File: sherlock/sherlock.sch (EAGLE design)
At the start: 24 parts, among them U3 XBEE-1B2, X1 2540-

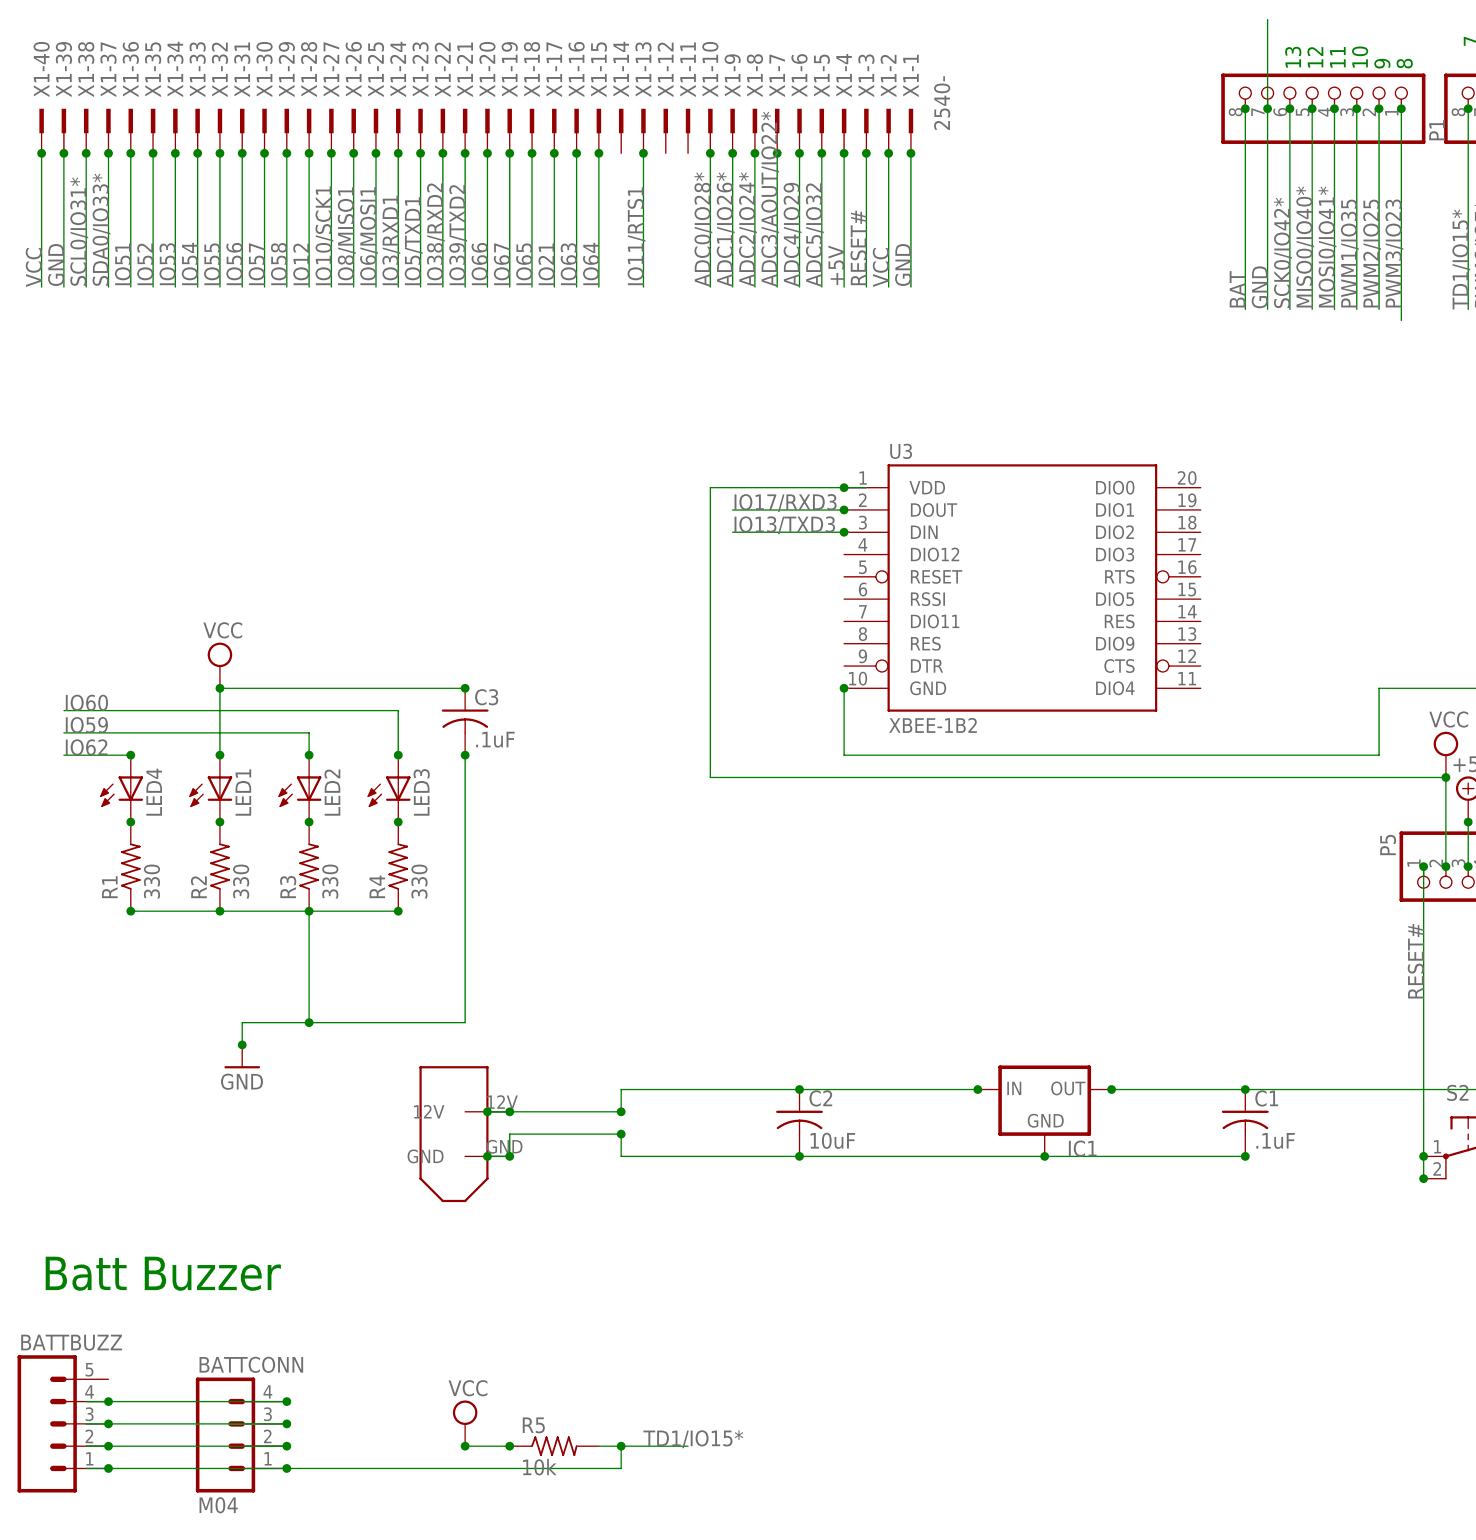
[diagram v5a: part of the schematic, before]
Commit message: Updated Sherlock, Watson & Solenoid Board to Rev D. Updated pie.lbr.
- Put SSOP16 footprint and symbol (from Sparkfun.lbr) in pie.lbr.
  Can be used as a template for any SSOP16 device.
- Created SSOP14 footprint and symbol in pie.lbr using SSOP16.
  Can be used as a template for any SSOP14 device.
- Added QUADNOR device to pie.lbr
- Added VCC and enable pin to solenoid connector on Watson
- Added enable pin for solenoid board on Sherlock
- Added quad-NOR gate onto Solenoid Board
- Added VCC and enable pin for quad-NOR gate on Solenoid Board
- Added 0.1uF capacitors between VCC&GND and 12V&GND for Solenoid Board
- Added mounting holes to Solenoid Board
- Added additional holes to Sherlock and Watson for the testing jig
- Replaced all holes with standoff part in pie.lbr
- Gave each hole a value, either "Mounting", "Test" or "Mounting + Test"
  to state their purpose.
- Added/copied devices on boards that were NOT in pie.lbr TO pie.lbr
- Removed unnecessary packages from copied devices
- Manually set pad diameters for through-hole packages that were
  added/created/already there for these three boards
- Added PARTNUMBER attribute to the library parts added/copied/
  created/already there for these three boards
- Moved all Sherlock passives to the top

RYAN: I fixed what you asked for this revision. If this goes
through, I will then work on fixing everything else you told me to.

Sherlock DFM: https://www.freedfm.com/freedfm/0019486703414971/results/summary2.htm
Watson DFM: https://www.freedfm.com/freedfm/0019486703414975/results/summary2.htm
Solenoid Board DFM: https://www.freedfm.com/freedfm/0019486703414973/results/summary2.htm

Change-Id: Ie6b1bdecadde8b7bc780ad23041f2e110bf24a4c
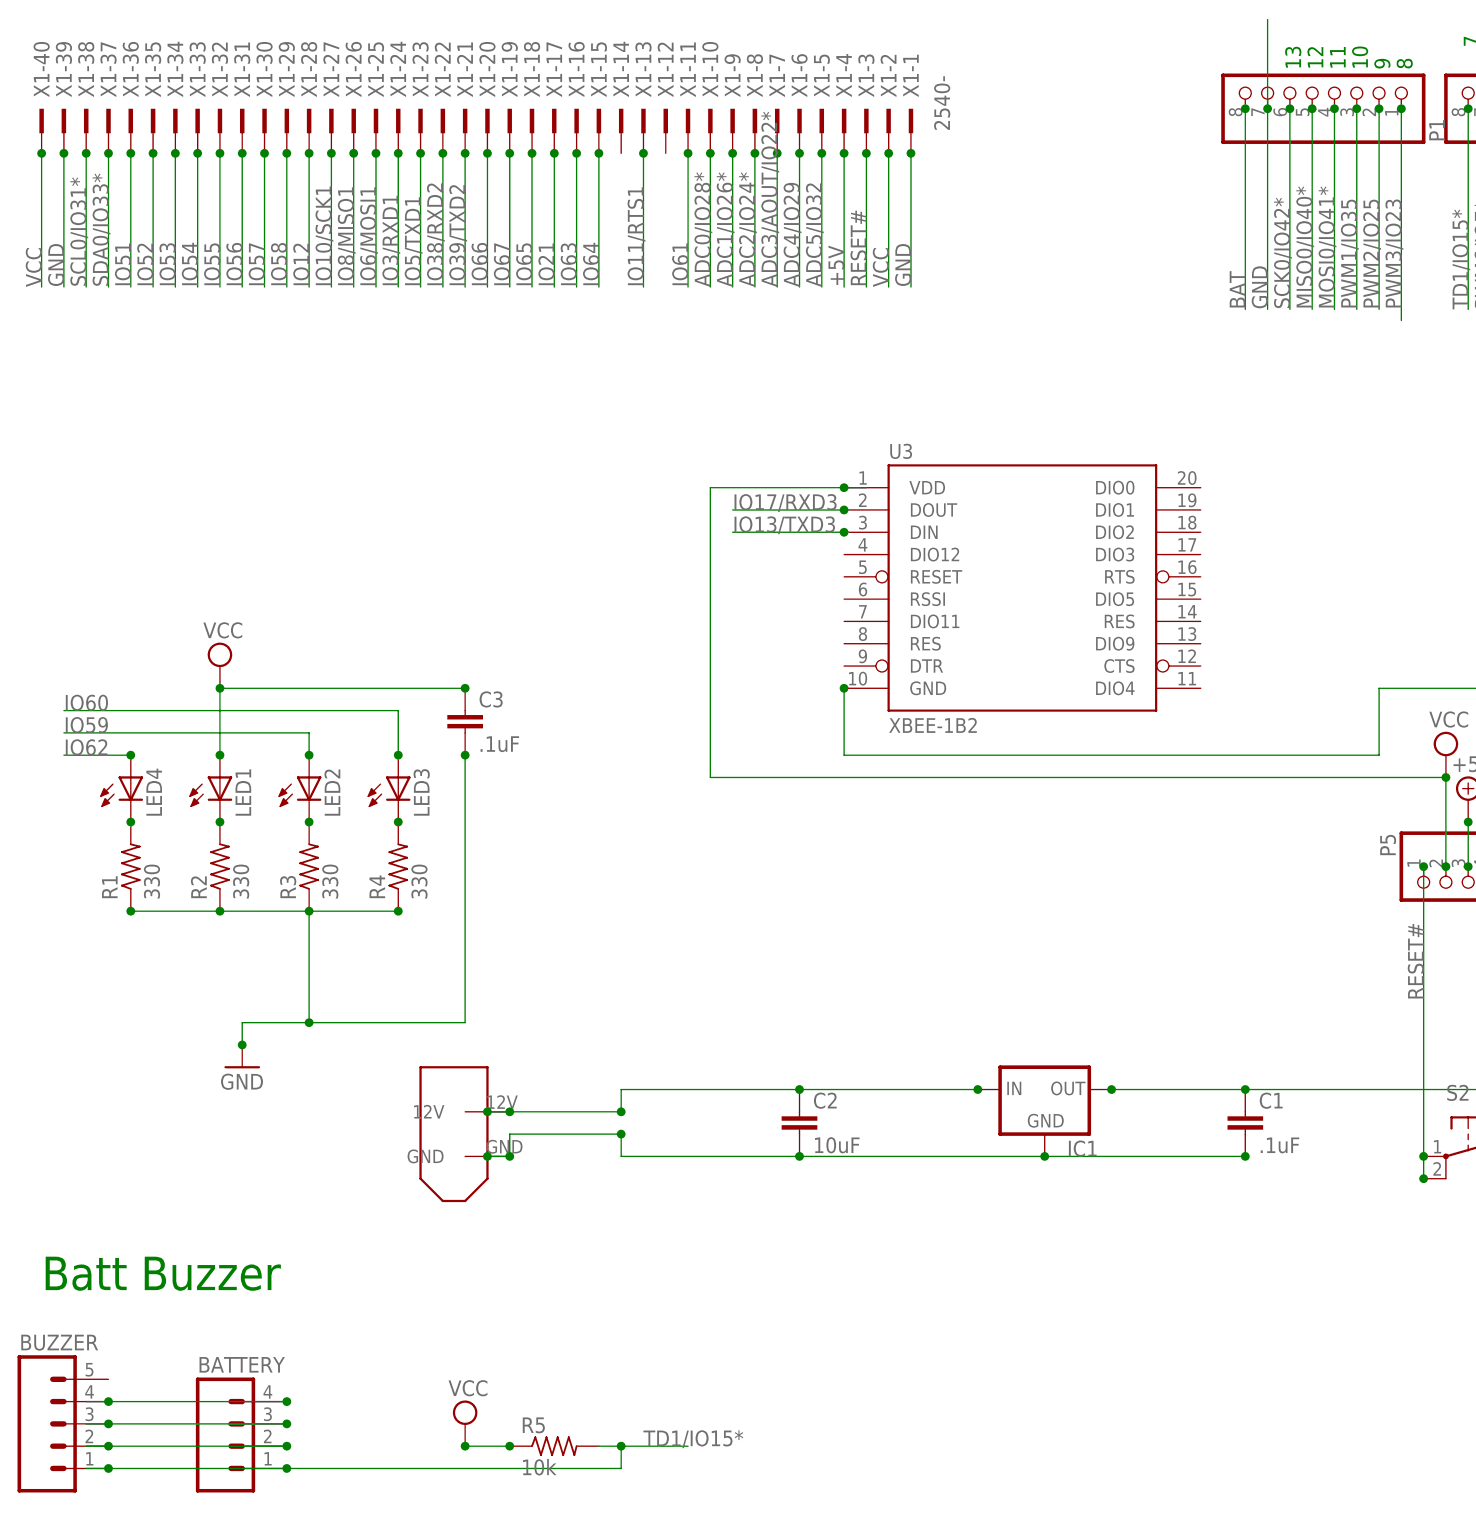
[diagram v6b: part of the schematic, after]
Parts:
- removed BATTBUZZ: (no value), SparkFun:M05PTH
- removed BATTCONN: M04, pie:M04
- added BATTERY: (no value), pie:M041X04-MTA
- added BUZZER: (no value), pie:M05PTH
- C1, C2: device rcl:C-USC0603 -> pie:CAP0603-CAP
- C3: device rcl:C-USC0603K -> pie:CAP0603-CAP
- IC1: device pie:78XXL -> pie:V_REG_78XXSIDE
- P1, P2: device pinhead-2:PINHD-1X08_2.54-S -> pie:PINHD-1X8
- P3: device pinhead:PINHD-2X20 -> pie:PINHD-2X20
- P4, P5: device pinhead-2:PINHD-1X06_2.54-S -> pie:PINHD-1X6
- R1, R2, R3, R4: device rcl:R-US_R0603 -> pie:R-US_R0603
- R5: device resistor:R-US_R0603 -> pie:R-US_R0603
- S2: device SparkFun:TAC_SWITCHPTH -> pie:TAC_SWITCHPTH
- U3: device SparkFun:XBEE-1B2 -> pie:XBEE-1B2
- X1: device con-3m:2540- -> pie:2540-
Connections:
- net IO61: now also X1-11.KL
- net N$5: now also BATTERY.4, BUZZER.4; no longer BATTBUZZ.4, BATTCONN.4
- net N$6: now also BATTERY.3, BUZZER.3; no longer BATTBUZZ.3, BATTCONN.3
- net N$7: now also BATTERY.2, BUZZER.2; no longer BATTBUZZ.2, BATTCONN.2
- net TD1/IO15*: now also BATTERY.1, BUZZER.1; no longer BATTBUZZ.1, BATTCONN.1
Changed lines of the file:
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@@
 </classes>
 <parts>
-<part name="P1" library="pinhead-2" deviceset="PINHD-1X08" device="_2.54-S"/>
-<part name="P2" library="pinhead-2" deviceset="PINHD-1X08" device="_2.54-S"/>
-<part name="P4" library="pinhead-2" deviceset="PINHD-1X06" device="_2.54-S"/>
-<part name="P5" library="pinhead-2" deviceset="PINHD-1X06" device="_2.54-S"/>
+<part name="P1" library="pie" deviceset="PINHD-1X8" device=""/>
+<part name="P2" library="pie" deviceset="PINHD-1X8" device=""/>
+<part name="P4" library="pie" deviceset="PINHD-1X6" device=""/>
+<part name="P5" library="pie" deviceset="PINHD-1X6" device=""/>
 <part name="GND2" library="supply1" deviceset="GND" device=""/>
 <part name="V17" library="supply2" deviceset="+5V" device=""/>
 <part name="V18" library="supply2" deviceset="VCC" device=""/>
-<part name="U3" library="SparkFun" deviceset="XBEE-1" device="B2"/>
-<part name="S2" library="SparkFun" deviceset="TAC_SWITCH" device="PTH"/>
+<part name="U3" library="pie" deviceset="XBEE-1" device="B2"/>
+<part name="S2" library="pie" deviceset="TAC_SWITCH" device="PTH"/>
 <part name="V1" library="supply2" deviceset="VCC" device=""/>
-<part name="P3" library="pinhead" deviceset="PINHD-2X20" device=""/>
+<part name="P3" library="pie" deviceset="PINHD-2X20" device=""/>
 <part name="GND3" library="supply1" deviceset="GND" device=""/>
-<part name="R1" library="rcl" deviceset="R-US_" device="R0603" value="330"/>
-<part name="R2" library="rcl" deviceset="R-US_" device="R0603" value="330"/>
-<part name="R3" library="rcl" deviceset="R-US_" device="R0603" value="330"/>
-<part name="R4" library="rcl" deviceset="R-US_" device="R0603" value="330"/>
-<part name="C3" library="rcl" deviceset="C-US" device="C0603K" value=".1uF"/>
-<part name="C1" library="rcl" deviceset="C-US" device="C0603" value=".1uF"/>
-<part name="IC1" library="pie" deviceset="78XXL" device=""/>
-<part name="X1" library="con-3m" deviceset="2540-" device="">
+<part name="R1" library="pie" deviceset="R-US_" device="R0603" value="330"/>
+<part name="R2" library="pie" deviceset="R-US_" device="R0603" value="330"/>
+<part name="R3" library="pie" deviceset="R-US_" device="R0603" value="330"/>
+<part name="R4" library="pie" deviceset="R-US_" device="R0603" value="330"/>
+<part name="C3" library="pie" deviceset="CAP" device="0603-CAP" value=".1uF"/>
+<part name="C1" library="pie" deviceset="CAP" device="0603-CAP" value=".1uF"/>
+<part name="IC1" library="pie" deviceset="V_REG_78XX" device="SIDE"/>
+<part name="X1" library="pie" deviceset="2540-" device="">
 <attribute name="OC_FARNELL" value="unknown"/>
 </part>
 <part name="U$1" library="pie" deviceset="XT60CONNECTOR" device=""/>
-<part name="BATTCONN" library="pie" deviceset="M04" device=""/>
-<part name="BATTBUZZ" library="SparkFun" deviceset="M05" device="PTH"/>
-<part name="R5" library="resistor" deviceset="R-US_" device="R0603" value="10k"/>
+<part name="BATTERY" library="pie" deviceset="M04" device="1X04-MTA"/>
+<part name="BUZZER" library="pie" deviceset="M05" device="PTH"/>
+<part name="R5" library="pie" deviceset="R-US_" device="R0603" value="10k"/>
 <part name="V2" library="supply2" deviceset="VCC" device=""/>
-<part name="C2" library="rcl" deviceset="C-US" device="C0603" value="10uF"/>
+<part name="C2" library="pie" deviceset="CAP" device="0603-CAP" value="10uF"/>
 <part name="FRAME1" library="pie" deviceset="FRAME-LETTER" device="">
 <attribute name="AUTHOR" value="Sahar M., Michael C., Sumita G."/>
-<attribute name="REVISION" value="C"/>
+<attribute name="REVISION" value="D"/>
 </part>
 <part name="LED4" library="pie" deviceset="LED" device="0805"/>
@@
 <instance part="R3" gate="G$1" x="43.18" y="83.82" rot="R90"/>
 <instance part="R4" gate="G$1" x="53.34" y="83.82" rot="R90"/>
-<instance part="C3" gate="G$1" x="60.96" y="101.6"/>
-<instance part="C1" gate="G$1" x="149.86" y="55.88"/>
-<instance part="IC1" gate="A" x="127" y="58.42"/>
+<instance part="C3" gate="G$1" x="60.96" y="99.06"/>
+<instance part="C1" gate="G$1" x="149.86" y="53.34"/>
+<instance part="IC1" gate="G$1" x="127" y="58.42"/>
 <instance part="X1" gate="-1" x="111.76" y="170.18" rot="R270"/>
 <instance part="X1" gate="-2" x="109.22" y="170.18" rot="R270"/>
@@
 <instance part="X1" gate="-40" x="12.7" y="170.18" rot="R270"/>
 <instance part="U$1" gate="G$1" x="55.88" y="60.96" rot="R270"/>
-<instance part="BATTCONN" gate="G$1" x="35.56" y="20.32"/>
-<instance part="BATTBUZZ" gate="G$1" x="12.7" y="20.32"/>
+<instance part="BATTERY" gate="G$1" x="35.56" y="17.78"/>
+<instance part="BUZZER" gate="G$1" x="12.7" y="20.32"/>
 <instance part="R5" gate="G$1" x="71.12" y="17.78"/>
 <instance part="V2" gate="G$1" x="60.96" y="20.32"/>
-<instance part="C2" gate="G$1" x="99.06" y="55.88"/>
+<instance part="C2" gate="G$1" x="99.06" y="53.34"/>
 <instance part="FRAME1" gate="G$1" x="0" y="0"/>
 <instance part="FRAME1" gate="G$2" x="147.32" y="0">
@@
 <pinref part="C1" gate="G$1" pin="2"/>
 <junction x="149.86" y="50.8"/>
-<pinref part="IC1" gate="A" pin="GND"/>
+<pinref part="IC1" gate="G$1" pin="GND"/>
 <wire x1="127" y1="50.8" x2="149.86" y2="50.8" width="0.1524" layer="91"/>
 <junction x="127" y="50.8"/>
@@
 <wire x1="149.86" y1="58.42" x2="182.88" y2="58.42" width="0.1524" layer="91"/>
 <junction x="149.86" y="58.42"/>
-<pinref part="IC1" gate="A" pin="OUT"/>
+<pinref part="IC1" gate="G$1" pin="OUT"/>
 <junction x="134.62" y="58.42"/>
 </segment>
@@
 </segment>
 <segment>
-<pinref part="BATTCONN" gate="G$1" pin="1"/>
+<pinref part="BATTERY" gate="G$1" pin="1"/>
 <wire x1="40.64" y1="15.24" x2="20.32" y2="15.24" width="0.1524" layer="91"/>
-<pinref part="BATTBUZZ" gate="G$1" pin="1"/>
+<pinref part="BUZZER" gate="G$1" pin="1"/>
 <junction x="20.32" y="15.24"/>
 <wire x1="20.32" y1="15.24" x2="17.78" y2="15.24" width="0.1524" layer="91"/>
@@
 <pinref part="P3" gate="A" pin="36"/>
 </segment>
+<segment>
+<pinref part="X1" gate="-11" pin="KL"/>
+<wire x1="86.36" y1="165.1" x2="86.36" y2="149.86" width="0.1524" layer="91"/>
+<junction x="86.36" y="165.1"/>
+<label x="86.36" y="149.86" size="1.778" layer="95" rot="R90"/>
+</segment>
 </net>
 <net name="IO63" class="0">
@@
 <wire x1="78.74" y1="58.42" x2="99.06" y2="58.42" width="0.1524" layer="91"/>
 <wire x1="99.06" y1="58.42" x2="119.38" y2="58.42" width="0.1524" layer="91"/>
-<pinref part="IC1" gate="A" pin="IN"/>
+<pinref part="IC1" gate="G$1" pin="IN"/>
 <junction x="119.38" y="58.42"/>
 <wire x1="78.74" y1="55.88" x2="78.74" y2="58.42" width="0.1524" layer="91"/>
@@
 <net name="N$5" class="0">
 <segment>
-<pinref part="BATTCONN" gate="G$1" pin="4"/>
+<pinref part="BATTERY" gate="G$1" pin="4"/>
 <wire x1="40.64" y1="22.86" x2="20.32" y2="22.86" width="0.1524" layer="91"/>
-<pinref part="BATTBUZZ" gate="G$1" pin="4"/>
+<pinref part="BUZZER" gate="G$1" pin="4"/>
 <junction x="20.32" y="22.86"/>
 <wire x1="20.32" y1="22.86" x2="17.78" y2="22.86" width="0.1524" layer="91"/>
@@
 <net name="N$6" class="0">
 <segment>
-<pinref part="BATTBUZZ" gate="G$1" pin="3"/>
-<pinref part="BATTCONN" gate="G$1" pin="3"/>
+<pinref part="BUZZER" gate="G$1" pin="3"/>
+<pinref part="BATTERY" gate="G$1" pin="3"/>
 <wire x1="20.32" y1="20.32" x2="40.64" y2="20.32" width="0.1524" layer="91"/>
 <wire x1="20.32" y1="20.32" x2="17.78" y2="20.32" width="0.1524" layer="91"/>
@@
 <segment>
 <wire x1="40.64" y1="17.78" x2="20.32" y2="17.78" width="0.1524" layer="91"/>
-<pinref part="BATTCONN" gate="G$1" pin="2"/>
+<pinref part="BATTERY" gate="G$1" pin="2"/>
 <wire x1="20.32" y1="17.78" x2="17.78" y2="17.78" width="0.1524" layer="91"/>
-<pinref part="BATTBUZZ" gate="G$1" pin="2"/>
+<pinref part="BUZZER" gate="G$1" pin="2"/>
 <junction x="20.32" y="17.78"/>
 <junction x="40.64" y="17.78"/>
